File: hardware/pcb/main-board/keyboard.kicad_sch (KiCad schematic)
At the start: 19 parts, among them U202 Unused 555

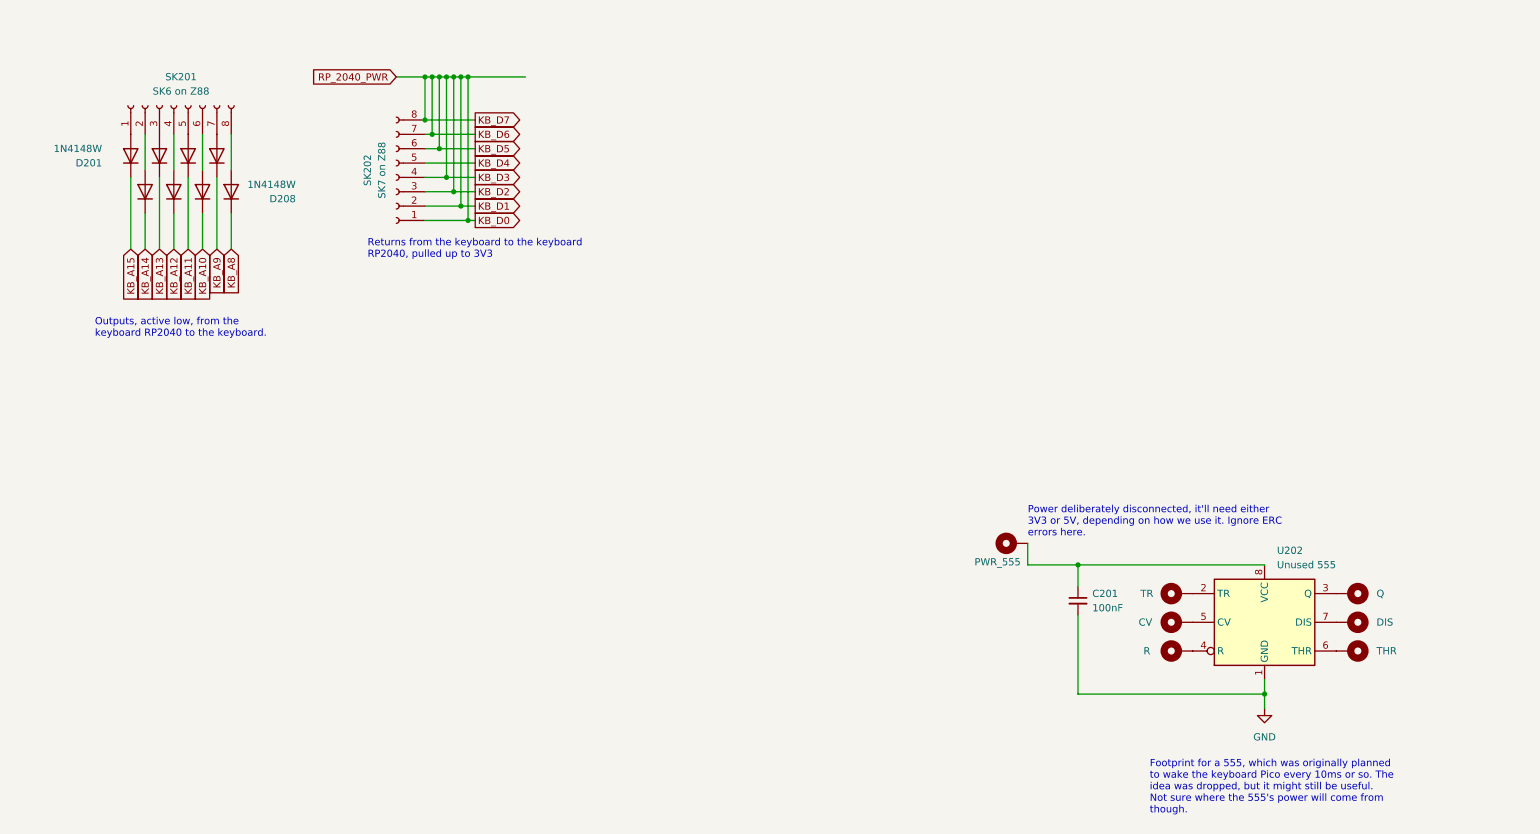
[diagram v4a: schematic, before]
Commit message: start the support pico rp2040 replacement
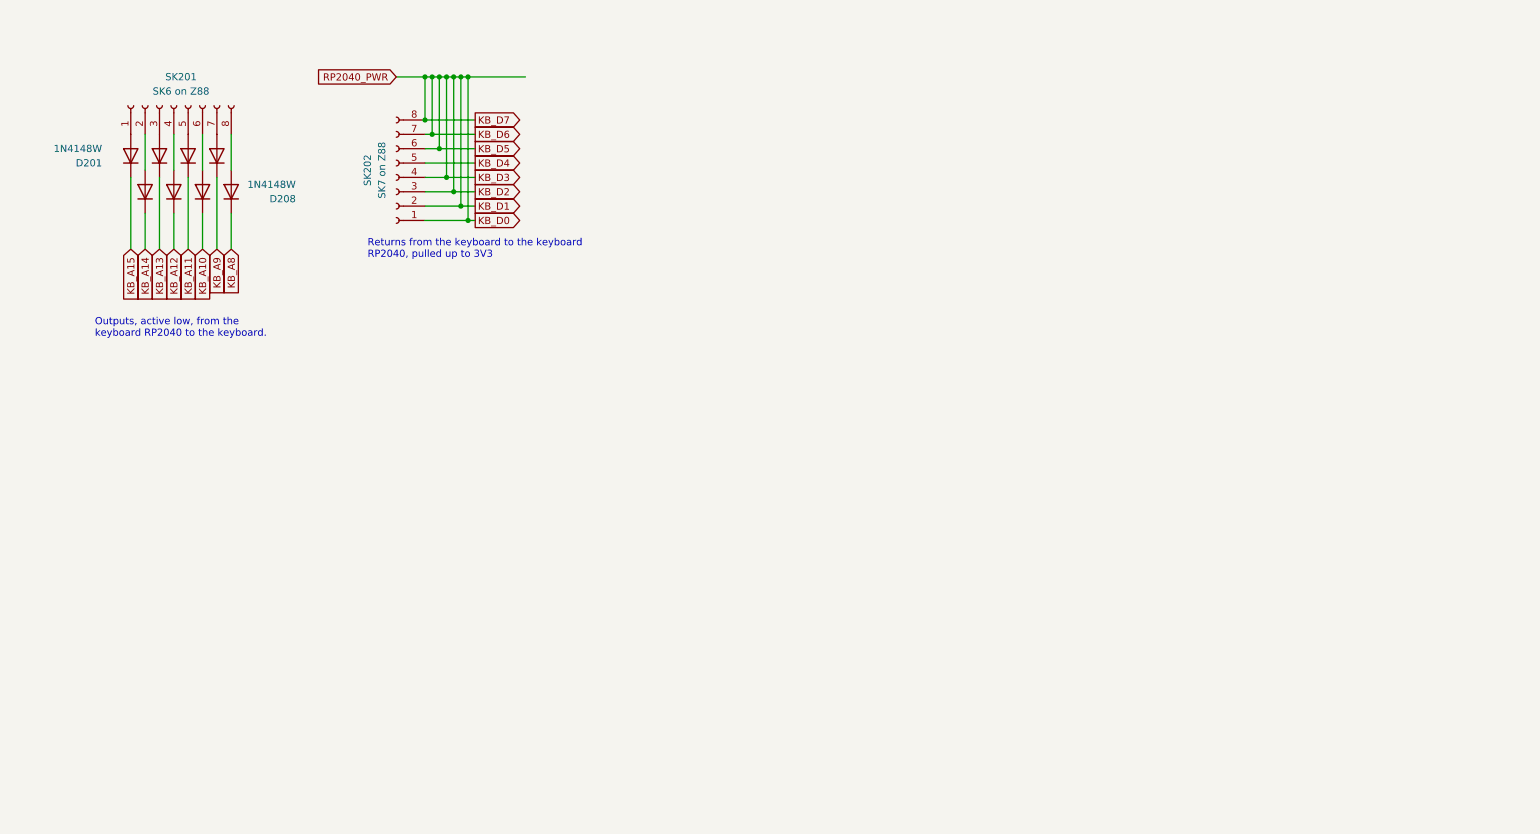
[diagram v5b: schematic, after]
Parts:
- removed C201: 100nF, Capacitor_SMD:C_0805_2012Metric_Pad1.18x1.45mm_HandSolder, symbol Device:C_Small
- removed H201: TR, Connector_Pin:Pin_D0.7mm_L6.5mm_W1.8mm_FlatFork, symbol Mechanical:MountingHole_Pad
- removed H202: CV, Connector_Pin:Pin_D0.7mm_L6.5mm_W1.8mm_FlatFork, symbol Mechanical:MountingHole_Pad
- removed H203: R, Connector_Pin:Pin_D0.7mm_L6.5mm_W1.8mm_FlatFork, symbol Mechanical:MountingHole_Pad
- removed H204: Q, Connector_Pin:Pin_D0.7mm_L6.5mm_W1.8mm_FlatFork, symbol Mechanical:MountingHole_Pad
- removed H205: DIS, Connector_Pin:Pin_D0.7mm_L6.5mm_W1.8mm_FlatFork, symbol Mechanical:MountingHole_Pad
- removed H206: THR, Connector_Pin:Pin_D0.7mm_L6.5mm_W1.8mm_FlatFork, symbol Mechanical:MountingHole_Pad
- removed H207: PWR_555, Connector_Pin:Pin_D0.7mm_L6.5mm_W1.8mm_FlatFork, symbol Mechanical:MountingHole_Pad
- removed U202: Unused 555, Package_SO:SOIC-8_3.9x4.9mm_P1.27mm, symbol Timer:LMC555xM
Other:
- note removed: "Footprint for a 555, which was originally planned to wake the keyboard Pico every 10ms or so. The idea was dropped, but it might still be useful. Not sure where the 555's power will come from though."
- note removed: "Power deliberately disconnected, it'll need either 3V3 or 5V, depending on how we use it. Ignore ERC errors here."

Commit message: a few more tidyups, almost ready for dual shifts stuff now
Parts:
- added H201: GND, MountingHole:MountingHole_2.2mm_M2_Pad, symbol Mechanical:MountingHole_Pad
- added R201, R202, R203, R204, R205, R206, R207: 1K2, symbol Device:R_Small
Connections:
- net KB_D0: now also R207.2; no longer SK202.2 (Pin_2), SK202.3 (Pin_3), SK202.4 (Pin_4), SK202.6 (Pin_6), SK202.7 (Pin_7), SK202.8 (Pin_8)
- new net DUAL_SHIFTS: H201.1
- new net KB_D1: R206.2, SK202.2 (Pin_2)
- new net KB_D2: R205.2, SK202.3 (Pin_3)
- new net KB_D3: R204.2, SK202.4 (Pin_4)
- new net KB_D5: R203.2, SK202.6 (Pin_6)
- new net KB_D6: R202.2, SK202.7 (Pin_7)
- new net KB_D7: R201.2, SK202.8 (Pin_8)
- new net RP2040_3V3_PWR: R201.1, R202.1, R203.1, R204.1, R205.1, R206.1, R207.1
